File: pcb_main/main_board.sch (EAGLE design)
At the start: 14 parts, among them U1 STM32F411RET6

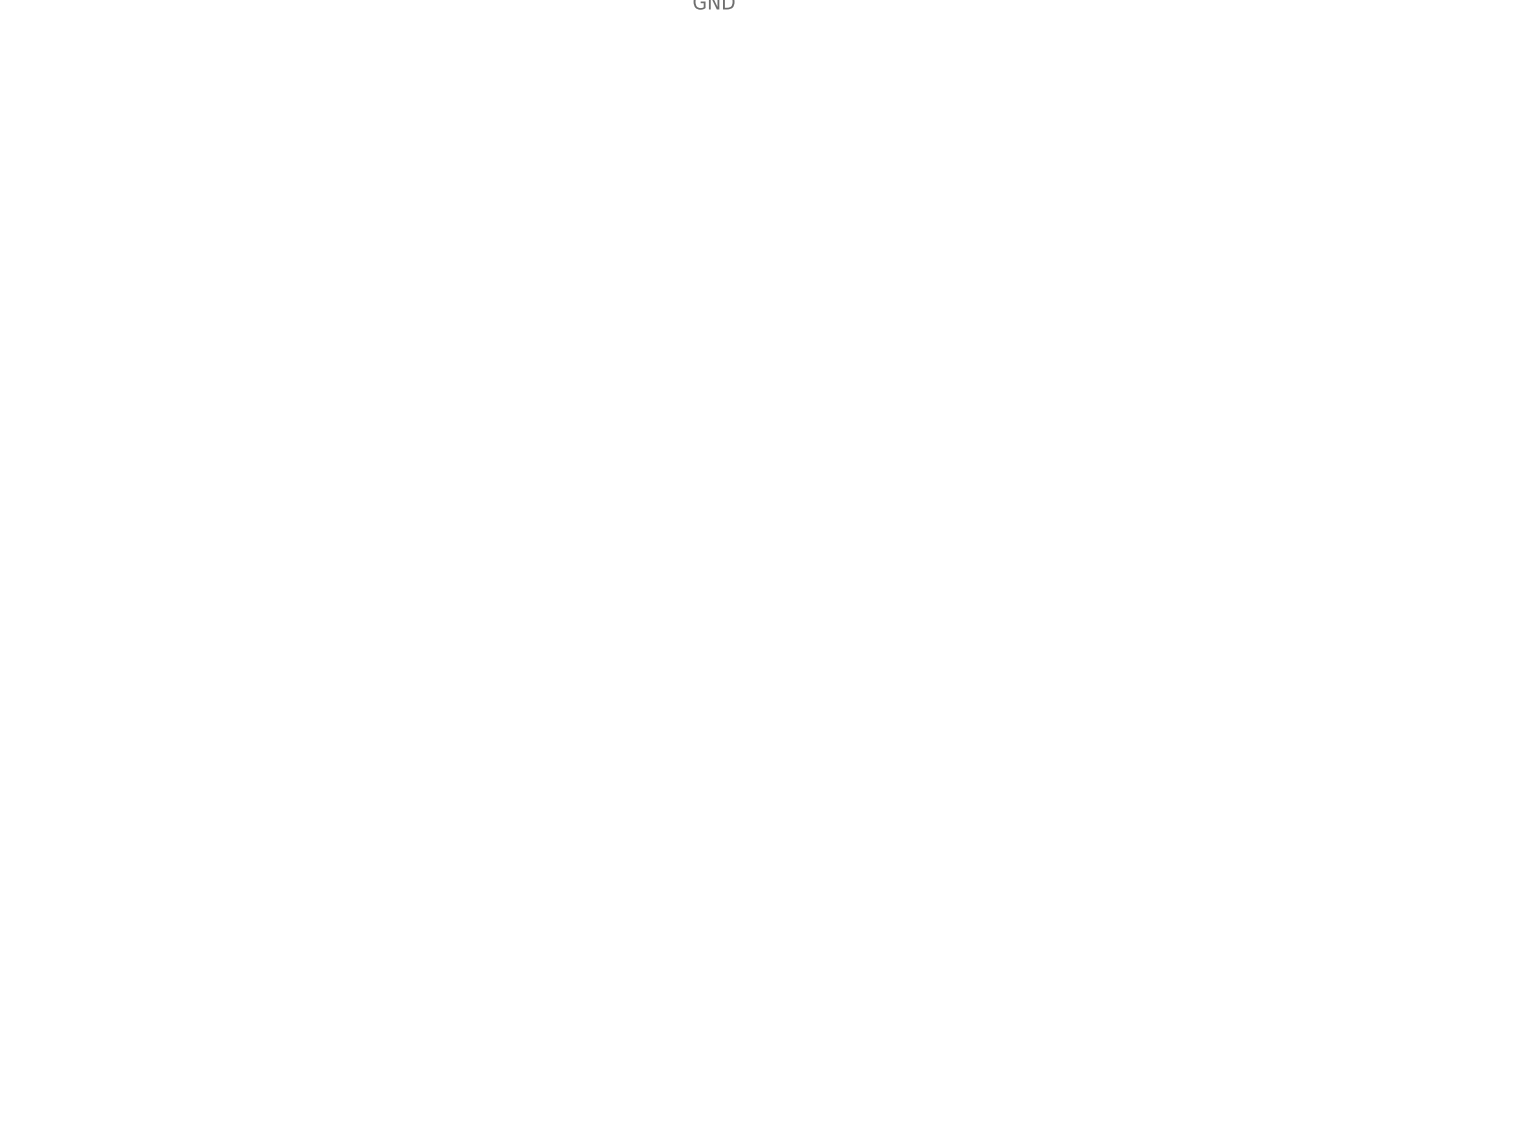
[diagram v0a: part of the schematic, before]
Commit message: sensors on main pcb
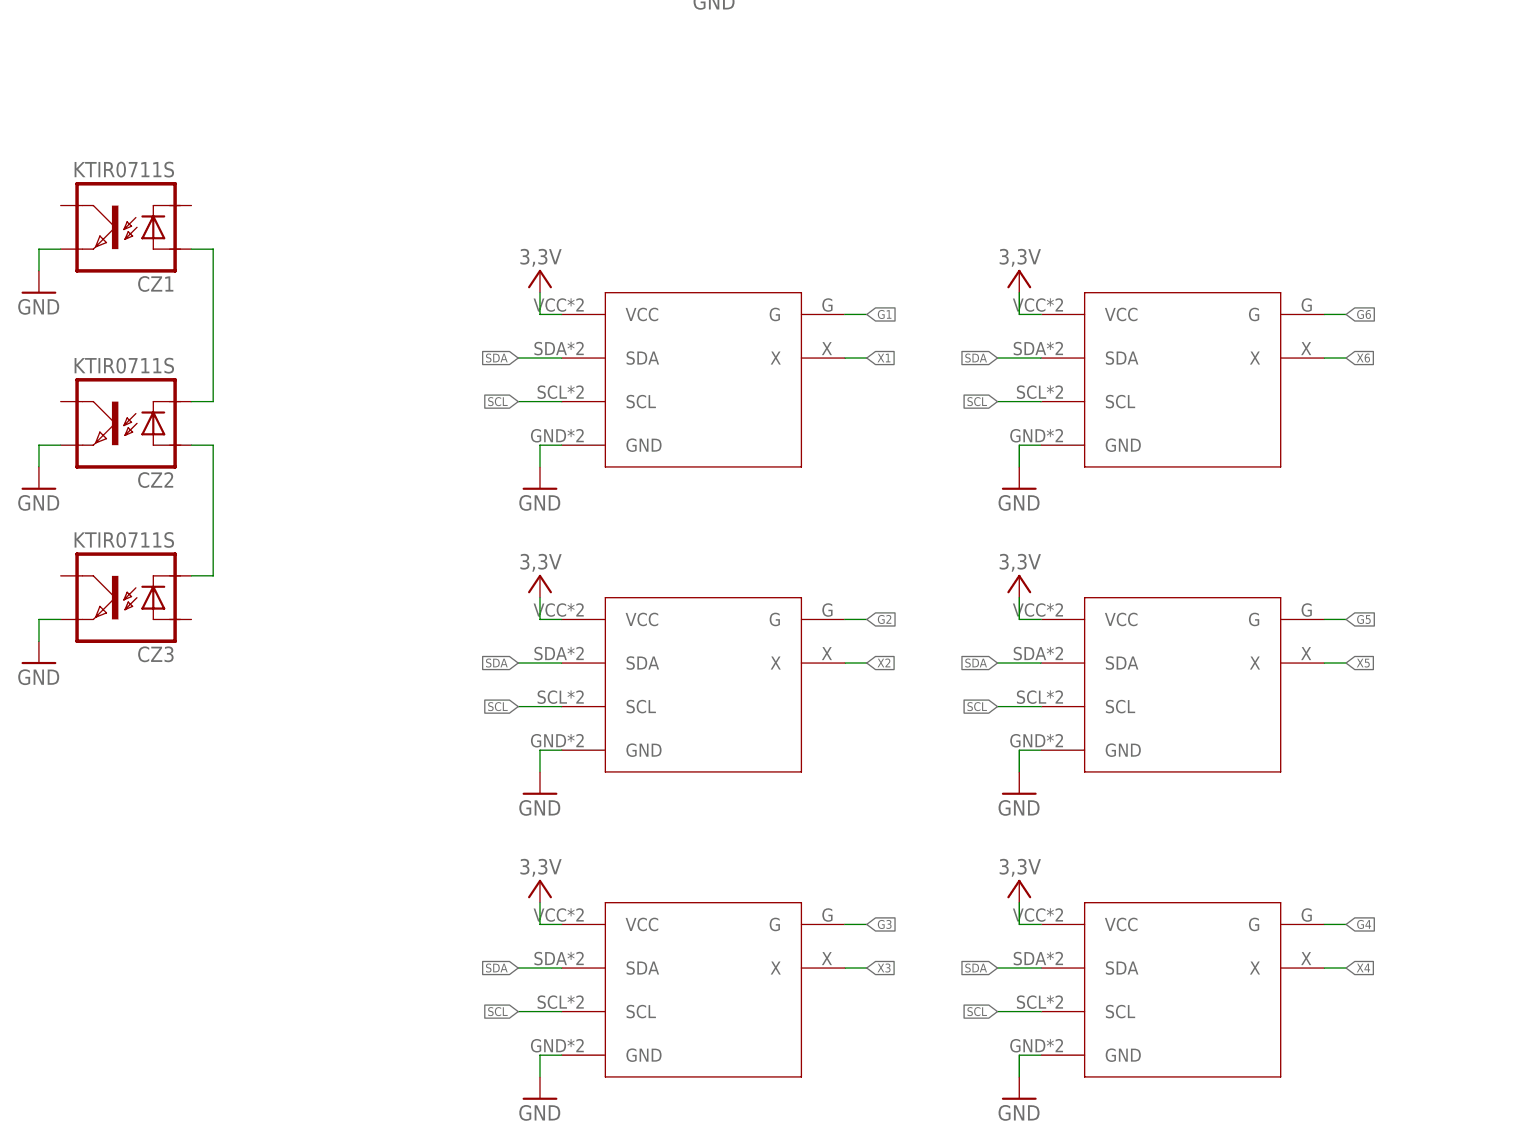
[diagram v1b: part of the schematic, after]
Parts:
- added CZ1, CZ2, CZ3: KTIR0711S, KTIR0711S:KTIR0711S
- added U$1, U$2, U$3, U$4, U$5, U$6: TOF_VL53L0X, TOF_VL53L0X:TOF_VL53L0X
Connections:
- new net G1: U$1.G
- new net G2: U$2.G
- new net G3: U$3.G
- new net G4: U$6.G
- new net G5: U$5.G
- new net G6: U$4.G
- new net N$3: CZ1.ANODA, CZ2.KATODA
- new net N$4: CZ2.ANODA, CZ3.KATODA
- new net SCL: U$1.SCL, U$2.SCL, U$3.SCL, U$4.SCL, U$5.SCL, U$6.SCL
- new net SDA: U$1.SDA, U$2.SDA, U$3.SDA, U$4.SDA, U$5.SDA, U$6.SDA
- new net X1: U$1.X
- new net X2: U$2.X
- new net X3: U$3.X
- new net X4: U$6.X
- new net X5: U$5.X
- new net X6: U$4.X
- net 3,3V: now also U$1.VCC, U$2.VCC, U$3.VCC, U$4.VCC, U$5.VCC, U$6.VCC
- net GND: now also CZ1.EMITER, CZ2.EMITER, CZ3.EMITER, U$1.GND, U$2.GND, U$3.GND, U$4.GND, U$5.GND, U$6.GND
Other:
- note added: "Distance sensors"

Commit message: pcb shape
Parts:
- removed LED1, LED2: (no value), led:LEDCHIP-LED0603
- added BATT: (no value), pinhead:PINHD-1X2
- added Q1: FDS5680, transistor-fet:FDS5680
- added Q2: 2N7002, 2N7002:2N7002
- added R3, R4, R5: (no value), rcl:R-EU_R0603
- added R6: 470R, rcl:R-EU_R0603
- added U$7: D24V10F3-H, D24V10F3:D24V10F3-H
- R2: value (none) -> 10k
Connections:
- net !A_DIR renamed A_DIR_1
- net A_DIR renamed A_DIR_2
- removed net +5V: C7.1, C8.+, TB6612.!STBY, TB6612.VCC
- removed net +BAT: C10.+, C9.1, TB6612.VM1, TB6612.VM2, TB6612.VM3
- new net BAT+: BATT.2, C10.+, C9.1, R1.2, TB6612.VM1, TB6612.VM2, TB6612.VM3, U$7.VIN
- new net BAT-: BATT.1, Q1.D
- new net LS1: CZ1.KOLEKTOR, R3.1
- new net LS2: CZ2.KOLEKTOR, R4.1
- new net LS3: CZ3.KOLEKTOR, R5.1
- new net LS_ON/OFF: R6.1
- new net N$5: Q2.G, R2.2, R6.2
- net 3,3V: now also C7.1, C8.+, R3.2, R4.2, R5.2, TB6612.!STBY, TB6612.VCC, U$7.VOUT
- net GND: now also Q1.S, Q2.S, R2.1, U$7.GND; no longer LED1.C, LED2.C
- net N$1: now also Q1.G; no longer LED1.A
- net N$2: now also CZ1.KATODA, Q2.D; no longer LED2.A, R2.1
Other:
- moved on the sheet: CZ1, CZ2, CZ3, R1, R2

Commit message: power routed more or less
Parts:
- added OLED: (no value), pinhead:PINHD-1X4
- added X1: FH12-14S-0.5SH, con-hirose:FH12-14S-0.5SH
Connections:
- net !B_DIR renamed B_DIR_1
- net B_DIR renamed B_DIR_2
- net LS_ON/OFF renamed LS_ON
- removed net N$1: Q1.G, R1.1
- new net LED: X1-7.1
- new net ROBOT_OFF: Q1.G, R1.1, X1-2.1
- new net RST: X1-8.1
- new net SW1: X1-3.1
- new net SW2: X1-4.1
- new net SW3: X1-5.1
- new net SW4: X1-6.1
- new net SWCLK: X1-10.1
- new net SWDIO: X1-9.1
- new net VCC: OLED.4
- net 3,3V: now also X1-14.1
- net GND: now also OLED.3, X1-1.1
- net SCL: now also OLED.2
- net SDA: now also OLED.1
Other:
- note added: "Line sensors"

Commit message: almost there
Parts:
- removed Q2: 2N7002, 2N7002:2N7002
- added C1, C2: 22p, rcl:C-EUC0603
- added C11, C12, C13, C15, C3, C6: 100n, rcl:C-EUC0603
- added C14, C5: 4u7, rcl:C-EUC0603
- added C4: 1u, rcl:C-EUC0603
- added JP1: (no value), pinhead:PINHD-1X3
- added R10, R11, R12, R13, R9: 4k7, rcl:R-EU_R0603
- added R14: 100R, rcl:R-EU_R0603
- added R7, R8: (no value), rcl:R-EU_R0603
- added S2: DTSM-3, switch-tact:DTSM-3
- added T1: BC847, transistor:BC847
- added U$8: 8MHz, CRYSTAL_SMD_3,4x2.7mm:CRYSTAL_3,4X2,7
- OLED: value (none) -> B4B-XH; device pinhead:PINHD-1X4 -> jst connectors:B4B-XH
- R1: value (none) -> 10k
- R2: value 10k -> 130R
- R6: value 470R -> 4k7
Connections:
- removed net 3,3V_ADC: U1.VDDA/VREF+
- removed net SCL: OLED.2, U$1.SCL, U$2.SCL, U$3.SCL, U$4.SCL, U$5.SCL, U$6.SCL
- removed net SDA: OLED.1, U$1.SDA, U$2.SDA, U$3.SDA, U$4.SDA, U$5.SDA, U$6.SDA
- new net BAT_MEAS: R7.2, R8.1, U1.PB1
- new net N$6: R2.1, T1.E
- new net N$7: U1.PB5
- new net RX: U1.PA3
- new net SCL_1: R10.1, U$1.SCL, U$2.SCL, U$3.SCL, U1.PB6
- new net SCL_2: OLED.2, R11.1, U1.PB10
- new net SCL_3: R13.1, U$4.SCL, U$5.SCL, U$6.SCL, U1.PA8
- new net SDA_1: R9.1, U$1.SDA, U$2.SDA, U$3.SDA, U1.PB7
- new net SDA_2: OLED.1, R6.1, U1.PB3
- new net SDA_3: R12.1, U$4.SDA, U$5.SDA, U$6.SDA, U1.PC9
- new net SERVO: JP1.3, U1.PA1
- new net TX: U1.PA2
- new net VCAP: C5.1, U1.VCAP1
- new net XTAL1: C2.1, U$8.1, U1.PH0-OSC_IN
- new net XTAL2: C1.1, U$8.3, U1.PH1-OSC_OUT
- net 3,3V: now also C11.1, C12.1, C13.1, C14.1, C3.1, C4.1, C6.1, OLED.4, R10.2, R11.2, R12.2, R13.2, R6.2, R9.2, U1.VDDA/VREF+, X1-1.1; no longer X1-14.1
- net A_DIR_1: now also U1.PC5
- net A_DIR_2: now also U1.PC4
- net BAT+: now also CZ3.ANODA, R7.1
- net B_DIR_1: now also U1.PB0
- net B_DIR_2: now also U1.PB2
- net GND: now also C1.2, C11.2, C12.2, C13.2, C14.2, C15.2, C2.2, C3.2, C4.2, C5.2, C6.2, JP1.1, R2.2, R8.2, S2.2, U$8.2, U1.BOOT0, X1-14.1; no longer Q2.S, R2.1, X1-1.1
- net LED: now also X1-8.1; no longer X1-7.1
- net LS1: now also U1.PC1
- net LS2: now also U1.PC2
- net LS3: now also U1.PC3
- net LS_ON: now also R14.1, U1.PC11; no longer R6.1
- net N$2: now also T1.C; no longer Q2.D
- net N$5: now also R14.2, T1.B; no longer Q2.G, R2.2, R6.2
- net PWMA: now also U1.PA6
- net PWMB: now also U1.PA7
- net ROBOT_OFF: now also X1-13.1; no longer X1-2.1
- net RST: now also C15.1, S2.1, U1.NRST, X1-7.1; no longer X1-8.1
- net SW1: now also X1-12.1; no longer X1-3.1
- net SW2: now also X1-11.1; no longer X1-4.1
- net SW3: now also X1-10.1; no longer X1-5.1
- net SW4: now also X1-9.1; no longer X1-6.1
- net SWCLK: now also U1.PA14, X1-5.1; no longer X1-10.1
- net SWDIO: now also U1.PA13, X1-6.1; no longer X1-9.1
- net VCC: now also JP1.2; no longer OLED.4
- net X1: now also U1.PC15-OSC32_OUT
- net X2: now also U1.PC14-OSC32_IN
- net X3: now also U1.PC13
- net X4: now also U1.PA12
- net X5: now also U1.PB14
- net X6: now also U1.PB13
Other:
- note added: "Power"
- note added: "dodać złącze na serwo, kondensatory pullupy do i2c uart"
- moved on the sheet: BATT, CZ1, CZ2, CZ3, Q1, R1, R2, R3, R4, R5, R6, U$7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

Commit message: before 2 H-bridges
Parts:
- added R15: 130R, rcl:R-EU_R0603
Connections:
- net 3,3V: now also R15.1
- net RST: now also R15.2
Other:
- moved on the sheet: C15, S2
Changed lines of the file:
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@@
 <part name="GND33" library="supply1" library_urn="urn:adsk.eagle:library:371" deviceset="GND" device=""/>
 <part name="GND34" library="supply1" library_urn="urn:adsk.eagle:library:371" deviceset="GND" device=""/>
+<part name="R15" library="rcl" library_urn="urn:adsk.eagle:library:334" deviceset="R-EU_" device="R0603" package3d_urn="urn:adsk.eagle:package:23555/3" value="130R"/>
+<part name="P+1" library="supply1" library_urn="urn:adsk.eagle:library:371" deviceset="VCC" device=""/>
 </parts>
 <sheets>
@@
 </instance>
 <instance part="P+24" gate="VCC" x="10.16" y="-116.84" smashed="yes"/>
-<instance part="S2" gate="G$1" x="101.6" y="17.78" smashed="yes" rot="R180">
-<attribute name="NAME" x="107.95" y="19.685" size="1.778" layer="95" rot="R270"/>
-<attribute name="VALUE" x="105.41" y="14.605" size="1.778" layer="96" rot="R270"/>
-</instance>
-<instance part="C15" gate="G$1" x="91.44" y="17.78" smashed="yes">
-<attribute name="NAME" x="92.964" y="18.161" size="1.778" layer="95"/>
-<attribute name="VALUE" x="92.964" y="13.081" size="1.778" layer="96"/>
+<instance part="S2" gate="G$1" x="101.6" y="15.24" smashed="yes" rot="R180">
+<attribute name="NAME" x="107.95" y="17.145" size="1.778" layer="95" rot="R270"/>
+<attribute name="VALUE" x="105.41" y="12.065" size="1.778" layer="96" rot="R270"/>
+</instance>
+<instance part="C15" gate="G$1" x="91.44" y="15.24" smashed="yes">
+<attribute name="NAME" x="92.964" y="15.621" size="1.778" layer="95"/>
+<attribute name="VALUE" x="92.964" y="10.541" size="1.778" layer="96"/>
 </instance>
 <instance part="GND33" gate="1" x="91.44" y="5.08" smashed="yes">
@@
 <attribute name="VALUE" x="99.06" y="2.54" size="1.778" layer="96"/>
 </instance>
+<instance part="R15" gate="G$1" x="96.52" y="30.48" smashed="yes" rot="R270">
+<attribute name="NAME" x="98.0186" y="34.29" size="1.778" layer="95" rot="R270"/>
+<attribute name="VALUE" x="93.218" y="34.29" size="1.778" layer="96" rot="R270"/>
+</instance>
+<instance part="P+1" gate="VCC" x="96.52" y="38.1" smashed="yes"/>
 </instances>
 <busses>
@@
 <pinref part="C15" gate="G$1" pin="2"/>
 <pinref part="GND33" gate="1" pin="GND"/>
-<wire x1="91.44" y1="12.7" x2="91.44" y2="7.62" width="0.1524" layer="91"/>
+<wire x1="91.44" y1="10.16" x2="91.44" y2="7.62" width="0.1524" layer="91"/>
 </segment>
 <segment>
 <pinref part="GND34" gate="1" pin="GND"/>
 <pinref part="S2" gate="G$1" pin="2"/>
-<wire x1="101.6" y1="7.62" x2="101.6" y2="12.7" width="0.1524" layer="91"/>
+<wire x1="101.6" y1="7.62" x2="101.6" y2="10.16" width="0.1524" layer="91"/>
 </segment>
 </net>
@@
 <label x="73.66" y="40.64" size="1.778" layer="95" rot="R180"/>
 </segment>
+<segment>
+<pinref part="R15" gate="G$1" pin="1"/>
+<pinref part="P+1" gate="VCC" pin="VCC"/>
+<label x="99.06" y="40.64" size="1.778" layer="95" rot="R180"/>
+</segment>
 </net>
 <net name="BO1" class="0">
@@
 <segment>
 <pinref part="S2" gate="G$1" pin="1"/>
-<wire x1="101.6" y1="22.86" x2="101.6" y2="30.48" width="0.1524" layer="91"/>
+<wire x1="101.6" y1="20.32" x2="101.6" y2="22.86" width="0.1524" layer="91"/>
 <pinref part="C15" gate="G$1" pin="1"/>
-<wire x1="101.6" y1="30.48" x2="91.44" y2="30.48" width="0.1524" layer="91"/>
-<wire x1="91.44" y1="30.48" x2="91.44" y2="20.32" width="0.1524" layer="91"/>
-<wire x1="101.6" y1="30.48" x2="109.22" y2="30.48" width="0.1524" layer="91"/>
-<junction x="101.6" y="30.48"/>
-<label x="109.22" y="30.48" size="1.016" layer="95" xref="yes"/>
-</segment>
-</net>
+<wire x1="101.6" y1="22.86" x2="96.52" y2="22.86" width="0.1524" layer="91"/>
+<wire x1="96.52" y1="22.86" x2="91.44" y2="22.86" width="0.1524" layer="91"/>
+<wire x1="91.44" y1="22.86" x2="91.44" y2="17.78" width="0.1524" layer="91"/>
+<wire x1="101.6" y1="22.86" x2="109.22" y2="22.86" width="0.1524" layer="91"/>
+<junction x="101.6" y="22.86"/>
+<label x="109.22" y="22.86" size="1.016" layer="95" xref="yes"/>
+<pinref part="R15" gate="G$1" pin="2"/>
+<wire x1="96.52" y1="25.4" x2="96.52" y2="22.86" width="0.1524" layer="91"/>
+<junction x="96.52" y="22.86"/>
+</segment>
+</net>
